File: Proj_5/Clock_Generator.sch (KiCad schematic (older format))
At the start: 9 parts, among them SW1 Reset Switch

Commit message: Dont be wonky:
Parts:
- gave numbers to parts that had none: 1
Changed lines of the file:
@@
 CLK_OUT
 $Comp
-L Device:C C?
+L Device:C C2
 U 1 1 5EA697DA
 P 2150 1250
-F 0 "C?" V 1898 1250 50  0000 C CNN
+F 0 "C2" V 1898 1250 50  0000 C CNN
 F 1 "0.1uF" V 1989 1250 50  0000 C CNN
 F 2 "" H 2188 1100 50  0001 C CNN

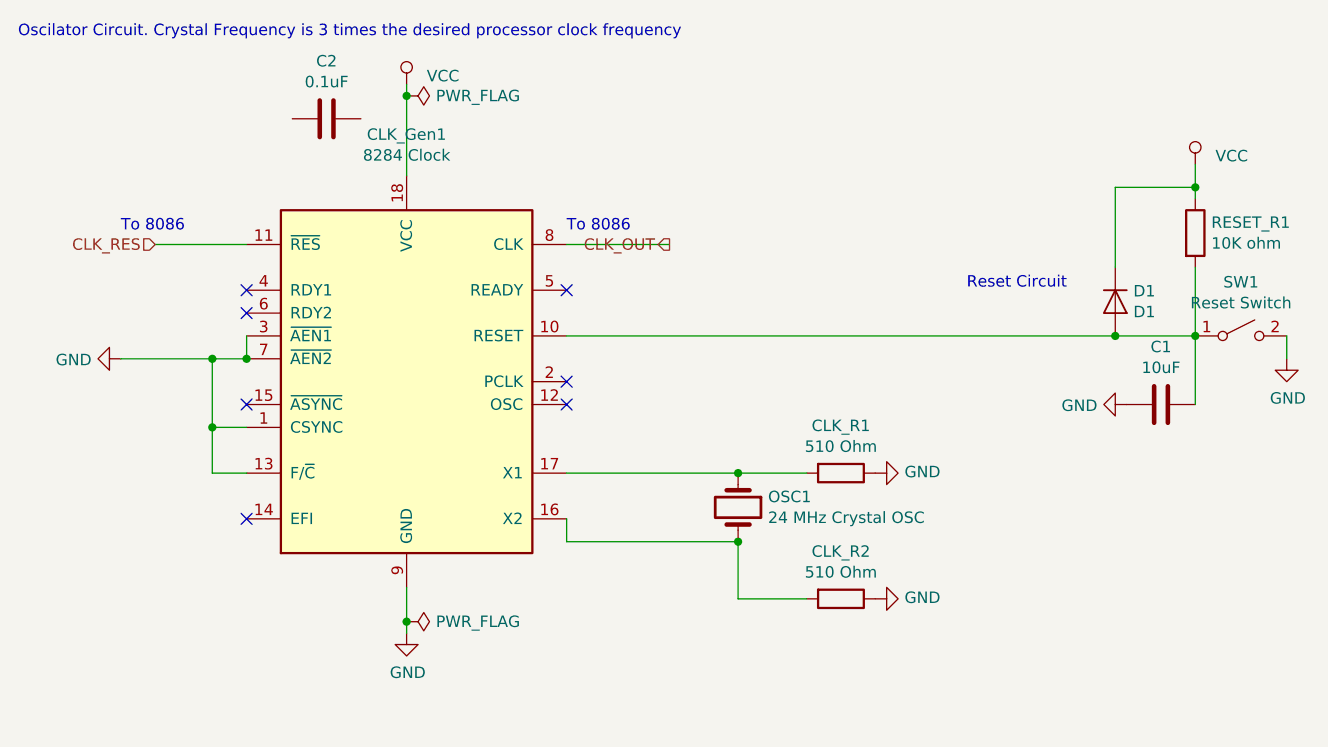
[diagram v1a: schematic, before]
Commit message: Changes to Top Level Connections
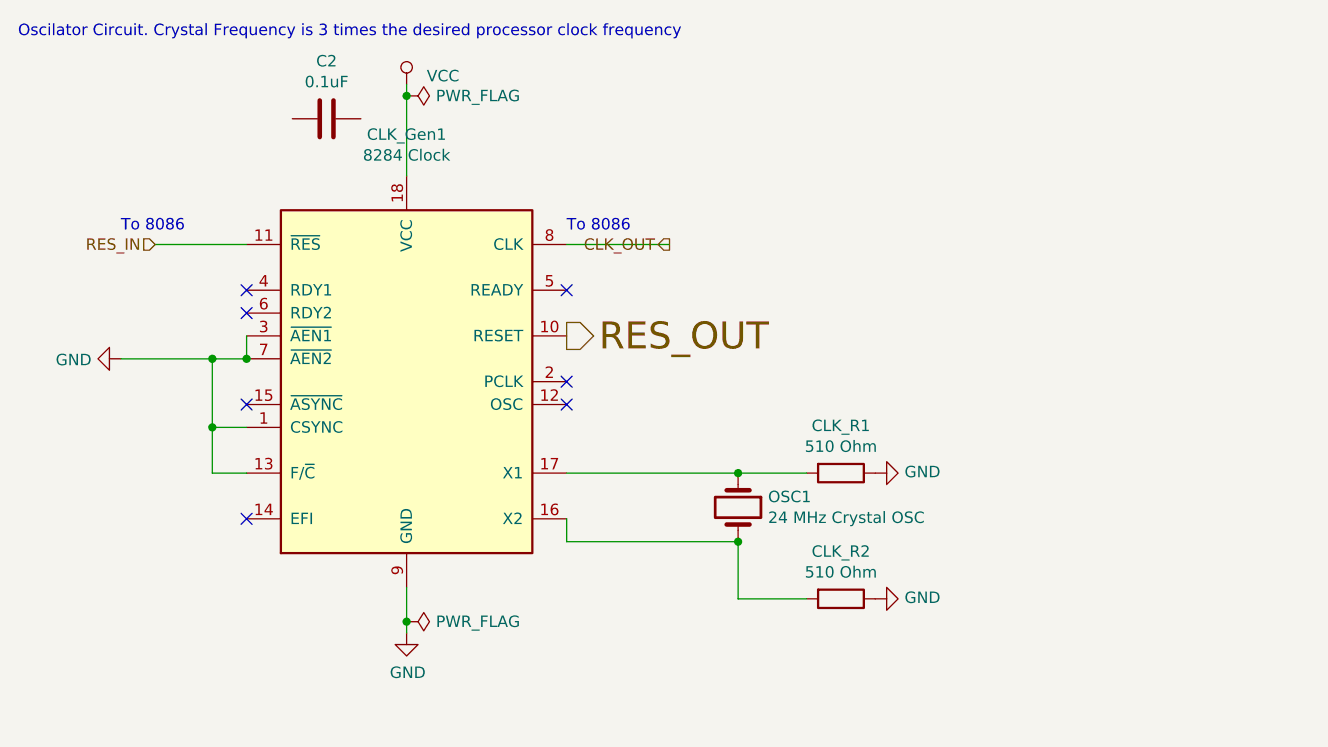
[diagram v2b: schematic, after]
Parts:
- removed C1: 10uF, symbol Device:C
- removed D1: D1, symbol Device:D
- removed RESET_R1: 10K ohm, symbol Device:R
- removed SW1: Reset Switch, symbol Switch:SW_SPST
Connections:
- net RES_OUT: now reaches CLK_Gen1.10 (RESET)
- net CLK_RES renamed RES_IN
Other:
- note removed: "Reset Circuit"
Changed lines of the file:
@@
 Wire Wire Line
 	3200 1800 3650 1800
-$Comp
-L Switch:SW_SPST SW?
-U 1 1 5EA0B868
-P 6150 2200
-AR Path="/5EA0B868" Ref="SW?"  Part="1"
-AR Path="/5E9E2E0E/5EA0B868" Ref="SW1"  Part="1"
-F 0 "SW1" H 6150 2435 50  0000 C CNN
-F 1 "Reset Switch" H 6150 2344 50  0000 C CNN
-F 2 "" H 6150 2200 50  0001 C CNN
-F 3 "~" H 6150 2200 50  0001 C CNN
-	1    6150 2200
-	1    0    0    -1
-$EndComp
-Connection ~ 5950 2200
-$Comp
-L Device:C C?
-U 1 1 5EA0B86F
-P 5800 2500
-AR Path="/5EA0B86F" Ref="C?"  Part="1"
-AR Path="/5E9E2E0E/5EA0B86F" Ref="C1"  Part="1"
-F 0 "C1" V 5548 2500 50  0000 C CNN
-F 1 "10uF" V 5639 2500 50  0000 C CNN
-F 2 "" H 5838 2350 50  0001 C CNN
-F 3 "~" H 5800 2500 50  0001 C CNN
-	1    5800 2500
-	0    1    1    0
-$EndComp
-Wire Wire Line
-	5950 2200 5950 2500
-$Comp
-L power:GND #PWR?
-U 1 1 5EA0B876
-P 5650 2500
-AR Path="/5EA0B876" Ref="#PWR?"  Part="1"
-AR Path="/5E9E2E0E/5EA0B876" Ref="#PWR0105"  Part="1"
-F 0 "#PWR0105" H 5650 2250 50  0001 C CNN
-F 1 "GND" V 5655 2372 50  0000 R CNN
-F 2 "" H 5650 2500 50  0001 C CNN
-F 3 "" H 5650 2500 50  0001 C CNN
-	1    5650 2500
-	0    1    1    0
-$EndComp
-Wire Wire Line
-	6350 2200 6350 2300
-$Comp
-L power:GND #PWR?
-U 1 1 5EA0B87D
-P 6350 2300
-AR Path="/5EA0B87D" Ref="#PWR?"  Part="1"
-AR Path="/5E9E2E0E/5EA0B87D" Ref="#PWR0106"  Part="1"
-F 0 "#PWR0106" H 6350 2050 50  0001 C CNN
-F 1 "GND" H 6355 2127 50  0000 C CNN
-F 2 "" H 6350 2300 50  0001 C CNN
-F 3 "" H 6350 2300 50  0001 C CNN
-	1    6350 2300
-	1    0    0    -1
-$EndComp
-$Comp
-L Device:R RESET_R?
-U 1 1 5EA0B883
-P 5950 1750
-AR Path="/5EA0B883" Ref="RESET_R?"  Part="1"
-AR Path="/5E9E2E0E/5EA0B883" Ref="RESET_R1"  Part="1"
-F 0 "RESET_R1" H 6020 1796 50  0000 L CNN
-F 1 "10K ohm" H 6020 1705 50  0000 L CNN
-F 2 "" V 5880 1750 50  0001 C CNN
-F 3 "~" H 5950 1750 50  0001 C CNN
-	1    5950 1750
-	1    0    0    -1
-$EndComp
-Wire Wire Line
-	3200 2200 5600 2200
-Wire Wire Line
-	5950 1900 5950 2200
-Wire Wire Line
-	5950 1600 5950 1550
-$Comp
-L power:VCC RESET_PWR?
-U 1 1 5EA0B88C
-P 5950 1450
-AR Path="/5EA0B88C" Ref="RESET_PWR?"  Part="1"
-AR Path="/5E9E2E0E/5EA0B88C" Ref="#RESET_PWR0101"  Part="1"
-F 0 "#RESET_PWR0101" H 5950 1300 50  0001 C CNN
-F 1 "VCC" H 6038 1487 50  0000 L CNN
-F 2 "" H 5950 1450 50  0001 C CNN
-F 3 "" H 5950 1450 50  0001 C CNN
-	1    5950 1450
-	1    0    0    -1
-$EndComp
-$Comp
-L Device:D D?
-U 1 1 5EA0B892
-P 5600 2050
-AR Path="/5EA0B892" Ref="D?"  Part="1"
-AR Path="/5E9E2E0E/5EA0B892" Ref="D1"  Part="1"
-F 0 "D1" V 5554 2129 50  0000 L CNN
-F 1 "D1" V 5645 2129 50  0000 L CNN
-F 2 "" H 5600 2050 50  0001 C CNN
-F 3 "~" H 5600 2050 50  0001 C CNN
-	1    5600 2050
-	0    1    1    0
-$EndComp
-Connection ~ 5600 2200
-Wire Wire Line
-	5600 2200 5950 2200
-Wire Wire Line
-	5600 1900 5600 1550
-Wire Wire Line
-	5600 1550 5950 1550
-Connection ~ 5950 1550
-Wire Wire Line
-	5950 1550 5950 1450
-Text Notes 4950 2000 0    50   ~ 0
-Reset Circuit
 NoConn ~ 1800 2000
 NoConn ~ 1800 2100
@@
 NoConn ~ 3200 2000
 Text HLabel 1400 1800 0    50   Input ~ 0
-CLK_RES
+RES_IN
 Text HLabel 3650 1800 0    50   Output ~ 0
 CLK_OUT
@@
 	0    1    1    0
 $EndComp
+Text HLabel 3200 2200 2    118  Output ~ 0
+RES_OUT
 $EndSCHEMATC

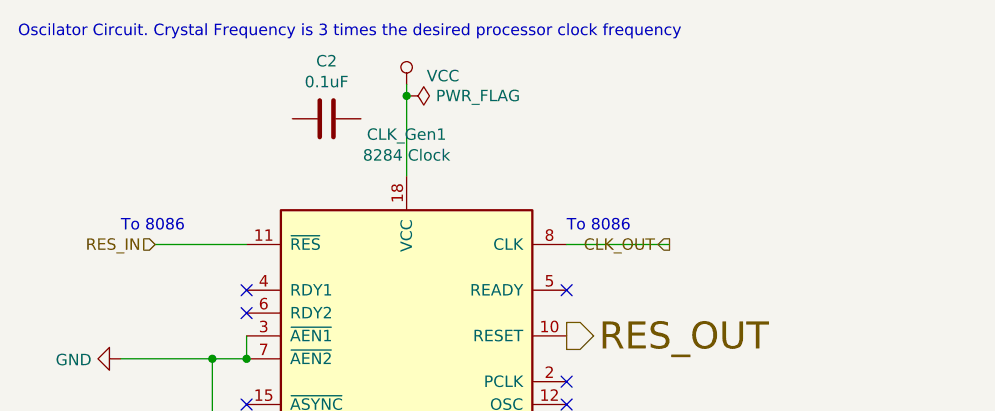
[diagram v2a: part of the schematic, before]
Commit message: Small changes to component placements.
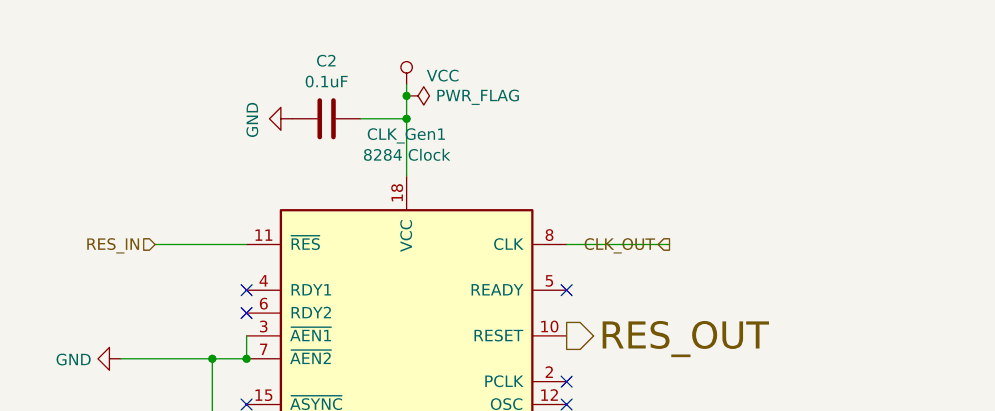
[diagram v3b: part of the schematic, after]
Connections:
- net GND: now also C2.2
- net VCC: now also C2.1
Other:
- note removed: "Oscilator Circuit. Crystal Frequency is 3 times the desired processor clock frequency"
- note removed: "To 8086 \n"
- note removed: "To 8086\n"
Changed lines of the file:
@@
 Connection ~ 2500 1150
 Wire Wire Line
-	2500 1150 2500 1500
+	2500 1150 2500 1250
 $Comp
 L power:GND #PWR?
@@
 	3950 3100 3950 3350
 Connection ~ 3950 3100
-Text Notes 800  900  0    50   ~ 0
-Oscilator Circuit. Crystal Frequency is 3 times the desired processor clock frequency
 Wire Wire Line
 	1800 2200 1800 2300
@@
 Wire Wire Line
 	1800 1800 1400 1800
-Text Notes 1250 1750 0    50   ~ 0
-To 8086 \n
-Text Notes 3200 1750 0    50   ~ 0
-To 8086\n
 Wire Wire Line
 	3200 1800 3650 1800
@@
 Text HLabel 3200 2200 2    118  Output ~ 0
 RES_OUT
+$Comp
+L power:GND #PWR?
+U 1 1 5EADFD76
+P 2000 1250
+AR Path="/5EADFD76" Ref="#PWR?"  Part="1"
+AR Path="/5E9E2E0E/5EADFD76" Ref="#PWR?"  Part="1"
+F 0 "#PWR?" H 2000 1000 50  0001 C CNN
+F 1 "GND" H 2005 1077 50  0000 C CNN
+F 2 "" H 2000 1250 50  0001 C CNN
+F 3 "" H 2000 1250 50  0001 C CNN
+	1    2000 1250
+	0    1    1    0
+$EndComp
+Wire Wire Line
+	2300 1250 2500 1250
+Connection ~ 2500 1250
+Wire Wire Line
+	2500 1250 2500 1500
 $EndSCHEMATC

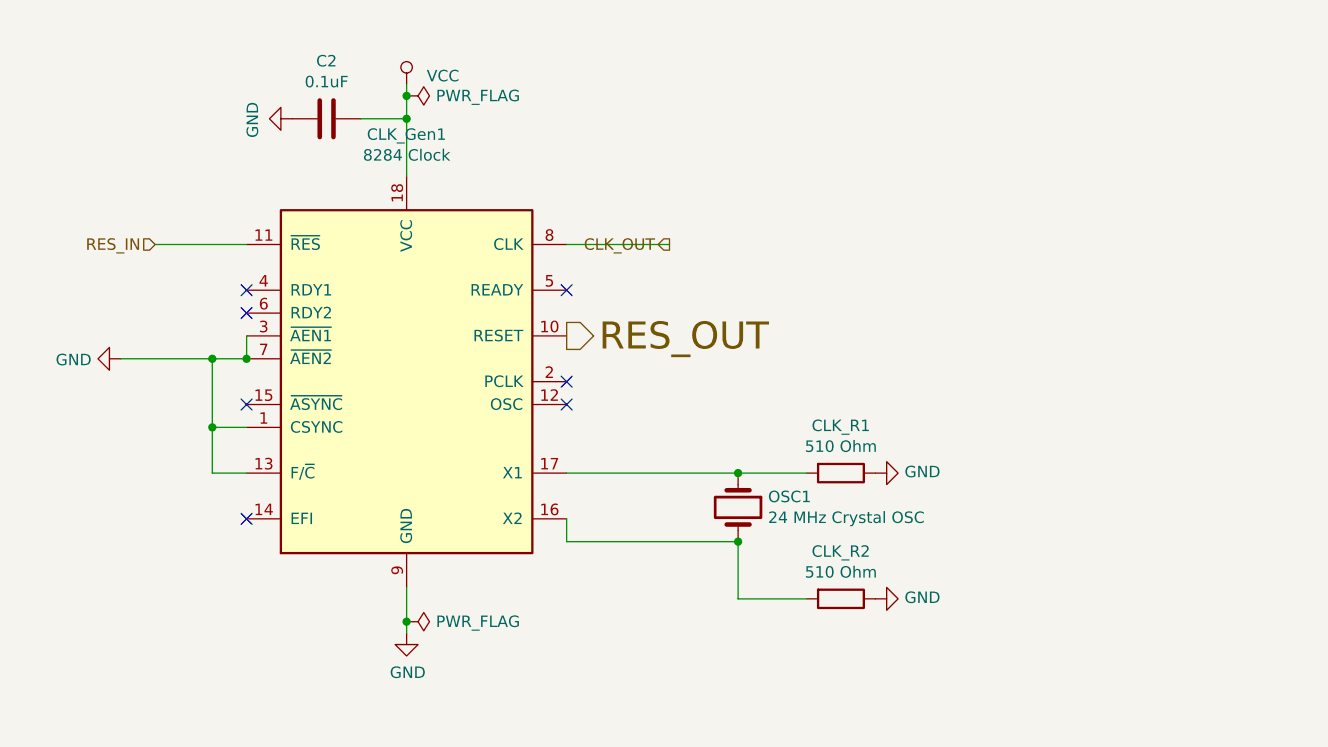
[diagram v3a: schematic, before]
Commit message: Added Power Flags, finished no connects.
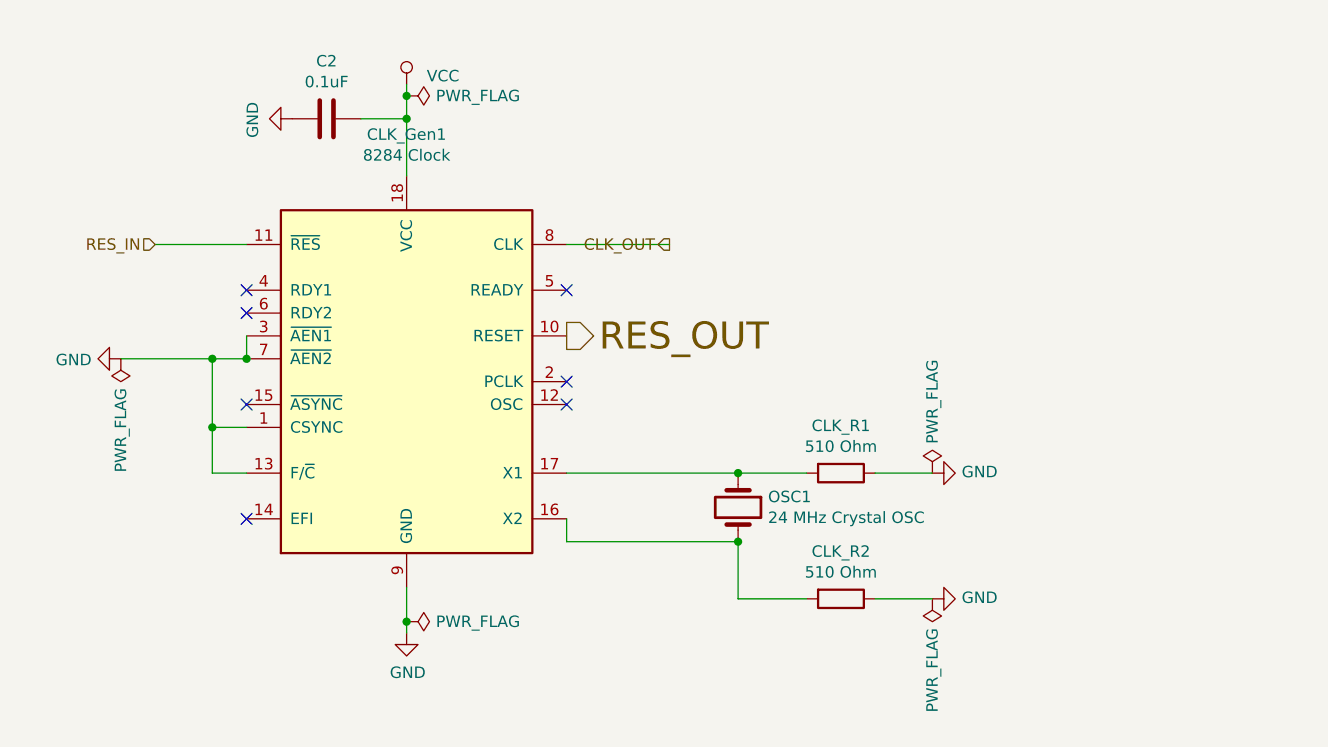
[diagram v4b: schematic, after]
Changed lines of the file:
@@
 $Descr A4 11693 8268
 encoding utf-8
-Sheet 2 9
+Sheet 2 10
 Title ""
 Date ""
@@
 L power:GND #PWR?
 U 1 1 5EA0B827
-P 4550 2800
+P 4800 2800
 AR Path="/5EA0B827" Ref="#PWR?"  Part="1"
 AR Path="/5E9E2E0E/5EA0B827" Ref="#PWR0101"  Part="1"
-F 0 "#PWR0101" H 4550 2550 50  0001 C CNN
-F 1 "GND" V 4555 2672 50  0000 R CNN
-F 2 "" H 4550 2800 50  0001 C CNN
-F 3 "" H 4550 2800 50  0001 C CNN
-	1    4550 2800
+F 0 "#PWR0101" H 4800 2550 50  0001 C CNN
+F 1 "GND" V 4805 2672 50  0000 R CNN
+F 2 "" H 4800 2800 50  0001 C CNN
+F 3 "" H 4800 2800 50  0001 C CNN
+	1    4800 2800
 	0    -1   -1   0
 $EndComp
@@
 L power:GND #PWR?
 U 1 1 5EA0B82D
-P 4550 3350
+P 4800 3350
 AR Path="/5EA0B82D" Ref="#PWR?"  Part="1"
 AR Path="/5E9E2E0E/5EA0B82D" Ref="#PWR0102"  Part="1"
-F 0 "#PWR0102" H 4550 3100 50  0001 C CNN
-F 1 "GND" V 4555 3222 50  0000 R CNN
-F 2 "" H 4550 3350 50  0001 C CNN
-F 3 "" H 4550 3350 50  0001 C CNN
-	1    4550 3350
+F 0 "#PWR0102" H 4800 3100 50  0001 C CNN
+F 1 "GND" V 4805 3222 50  0000 R CNN
+F 2 "" H 4800 3350 50  0001 C CNN
+F 3 "" H 4800 3350 50  0001 C CNN
+	1    4800 3350
 	0    -1   -1   0
 $EndComp
@@
 P 2000 1250
 AR Path="/5EADFD76" Ref="#PWR?"  Part="1"
-AR Path="/5E9E2E0E/5EADFD76" Ref="#PWR?"  Part="1"
-F 0 "#PWR?" H 2000 1000 50  0001 C CNN
+AR Path="/5E9E2E0E/5EADFD76" Ref="#PWR03"  Part="1"
+F 0 "#PWR03" H 2000 1000 50  0001 C CNN
 F 1 "GND" H 2005 1077 50  0000 C CNN
 F 2 "" H 2000 1250 50  0001 C CNN
@@
 Wire Wire Line
 	2500 1250 2500 1500
+Wire Wire Line
+	4550 2800 4800 2800
+Wire Wire Line
+	4550 3350 4800 3350
+$Comp
+L power:PWR_FLAG #FLG?
+U 1 1 5F9B7B42
+P 4800 3350
+AR Path="/5EAF7226/5F9B7B42" Ref="#FLG?"  Part="1"
+AR Path="/5E9E2E0E/5F9B7B42" Ref="#FLG03"  Part="1"
+F 0 "#FLG03" H 4800 3425 50  0001 C CNN
+F 1 "PWR_FLAG" V 4800 3478 50  0000 L CNN
+F 2 "" H 4800 3350 50  0001 C CNN
+F 3 "~" H 4800 3350 50  0001 C CNN
+	1    4800 3350
+	-1   0    0    1
+$EndComp
+$Comp
+L power:PWR_FLAG #FLG?
+U 1 1 5F9B832D
+P 4800 2800
+AR Path="/5EAF7226/5F9B832D" Ref="#FLG?"  Part="1"
+AR Path="/5E9E2E0E/5F9B832D" Ref="#FLG02"  Part="1"
+F 0 "#FLG02" H 4800 2875 50  0001 C CNN
+F 1 "PWR_FLAG" V 4800 2928 50  0000 L CNN
+F 2 "" H 4800 2800 50  0001 C CNN
+F 3 "~" H 4800 2800 50  0001 C CNN
+	1    4800 2800
+	1    0    0    -1
+$EndComp
+$Comp
+L power:PWR_FLAG #FLG?
+U 1 1 5F9B8A93
+P 1250 2300
+AR Path="/5EAF7226/5F9B8A93" Ref="#FLG?"  Part="1"
+AR Path="/5E9E2E0E/5F9B8A93" Ref="#FLG01"  Part="1"
+F 0 "#FLG01" H 1250 2375 50  0001 C CNN
+F 1 "PWR_FLAG" V 1250 2428 50  0000 L CNN
+F 2 "" H 1250 2300 50  0001 C CNN
+F 3 "~" H 1250 2300 50  0001 C CNN
+	1    1250 2300
+	-1   0    0    1
+$EndComp
 $EndSCHEMATC

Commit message: Power Flags
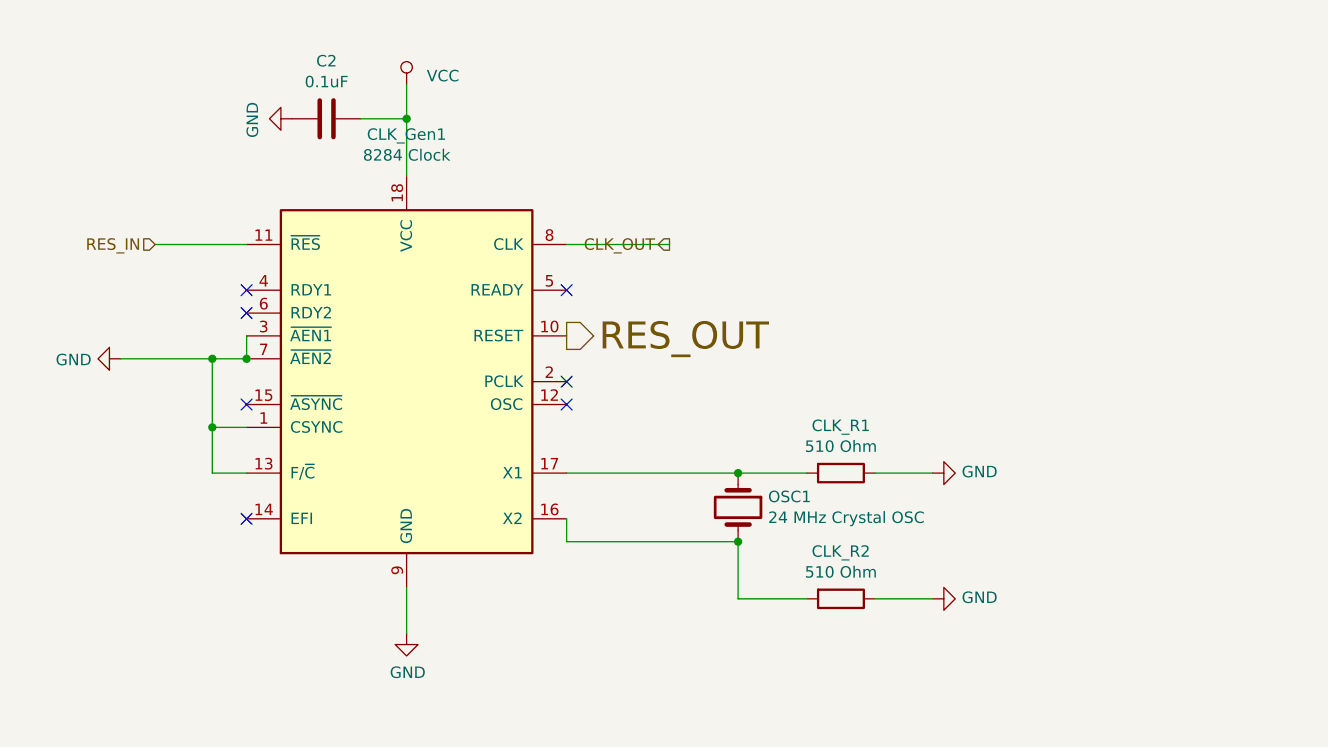
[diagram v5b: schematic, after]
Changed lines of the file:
@@
 	1    0    0    -1
 $EndComp
-Wire Wire Line
-	2500 1100 2500 1150
-$Comp
-L power:PWR_FLAG #FLG?
-U 1 1 5EA0B83A
-P 2500 1150
-AR Path="/5EA0B83A" Ref="#FLG?"  Part="1"
-AR Path="/5E9E2E0E/5EA0B83A" Ref="#FLG0101"  Part="1"
-F 0 "#FLG0101" H 2500 1225 50  0001 C CNN
-F 1 "PWR_FLAG" V 2500 1278 50  0000 L CNN
-F 2 "" H 2500 1150 50  0001 C CNN
-F 3 "~" H 2500 1150 50  0001 C CNN
-	1    2500 1150
-	0    1    1    0
-$EndComp
-Connection ~ 2500 1150
-Wire Wire Line
-	2500 1150 2500 1250
 $Comp
 L power:GND #PWR?
@@
 	1    0    0    -1
 $EndComp
-Wire Wire Line
-	2500 3300 2500 3450
-$Comp
-L power:PWR_FLAG #FLG?
-U 1 1 5EA0B849
-P 2500 3450
-AR Path="/5EA0B849" Ref="#FLG?"  Part="1"
-AR Path="/5E9E2E0E/5EA0B849" Ref="#FLG0102"  Part="1"
-F 0 "#FLG0102" H 2500 3525 50  0001 C CNN
-F 1 "PWR_FLAG" V 2500 3578 50  0000 L CNN
-F 2 "" H 2500 3450 50  0001 C CNN
-F 3 "~" H 2500 3450 50  0001 C CNN
-	1    2500 3450
-	0    1    1    0
-$EndComp
-Connection ~ 2500 3450
-Wire Wire Line
-	2500 3450 2500 3500
 Wire Wire Line
 	3950 3100 3950 3350
@@
 	4550 2800 4800 2800
 Wire Wire Line
+	2500 1100 2500 1250
+Wire Wire Line
 	4550 3350 4800 3350
-$Comp
-L power:PWR_FLAG #FLG?
-U 1 1 5F9B7B42
-P 4800 3350
-AR Path="/5EAF7226/5F9B7B42" Ref="#FLG?"  Part="1"
-AR Path="/5E9E2E0E/5F9B7B42" Ref="#FLG03"  Part="1"
-F 0 "#FLG03" H 4800 3425 50  0001 C CNN
-F 1 "PWR_FLAG" V 4800 3478 50  0000 L CNN
-F 2 "" H 4800 3350 50  0001 C CNN
-F 3 "~" H 4800 3350 50  0001 C CNN
-	1    4800 3350
-	-1   0    0    1
-$EndComp
-$Comp
-L power:PWR_FLAG #FLG?
-U 1 1 5F9B832D
-P 4800 2800
-AR Path="/5EAF7226/5F9B832D" Ref="#FLG?"  Part="1"
-AR Path="/5E9E2E0E/5F9B832D" Ref="#FLG02"  Part="1"
-F 0 "#FLG02" H 4800 2875 50  0001 C CNN
-F 1 "PWR_FLAG" V 4800 2928 50  0000 L CNN
-F 2 "" H 4800 2800 50  0001 C CNN
-F 3 "~" H 4800 2800 50  0001 C CNN
-	1    4800 2800
-	1    0    0    -1
-$EndComp
-$Comp
-L power:PWR_FLAG #FLG?
-U 1 1 5F9B8A93
-P 1250 2300
-AR Path="/5EAF7226/5F9B8A93" Ref="#FLG?"  Part="1"
-AR Path="/5E9E2E0E/5F9B8A93" Ref="#FLG01"  Part="1"
-F 0 "#FLG01" H 1250 2375 50  0001 C CNN
-F 1 "PWR_FLAG" V 1250 2428 50  0000 L CNN
-F 2 "" H 1250 2300 50  0001 C CNN
-F 3 "~" H 1250 2300 50  0001 C CNN
-	1    1250 2300
-	-1   0    0    1
-$EndComp
+Wire Wire Line
+	2500 3300 2500 3500
 $EndSCHEMATC
